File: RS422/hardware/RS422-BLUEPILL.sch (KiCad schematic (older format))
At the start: 9 parts, among them P2 RJ45, P3 RJ45, U1 BLUE-PILL, U2 SN75179, U3 SN75179

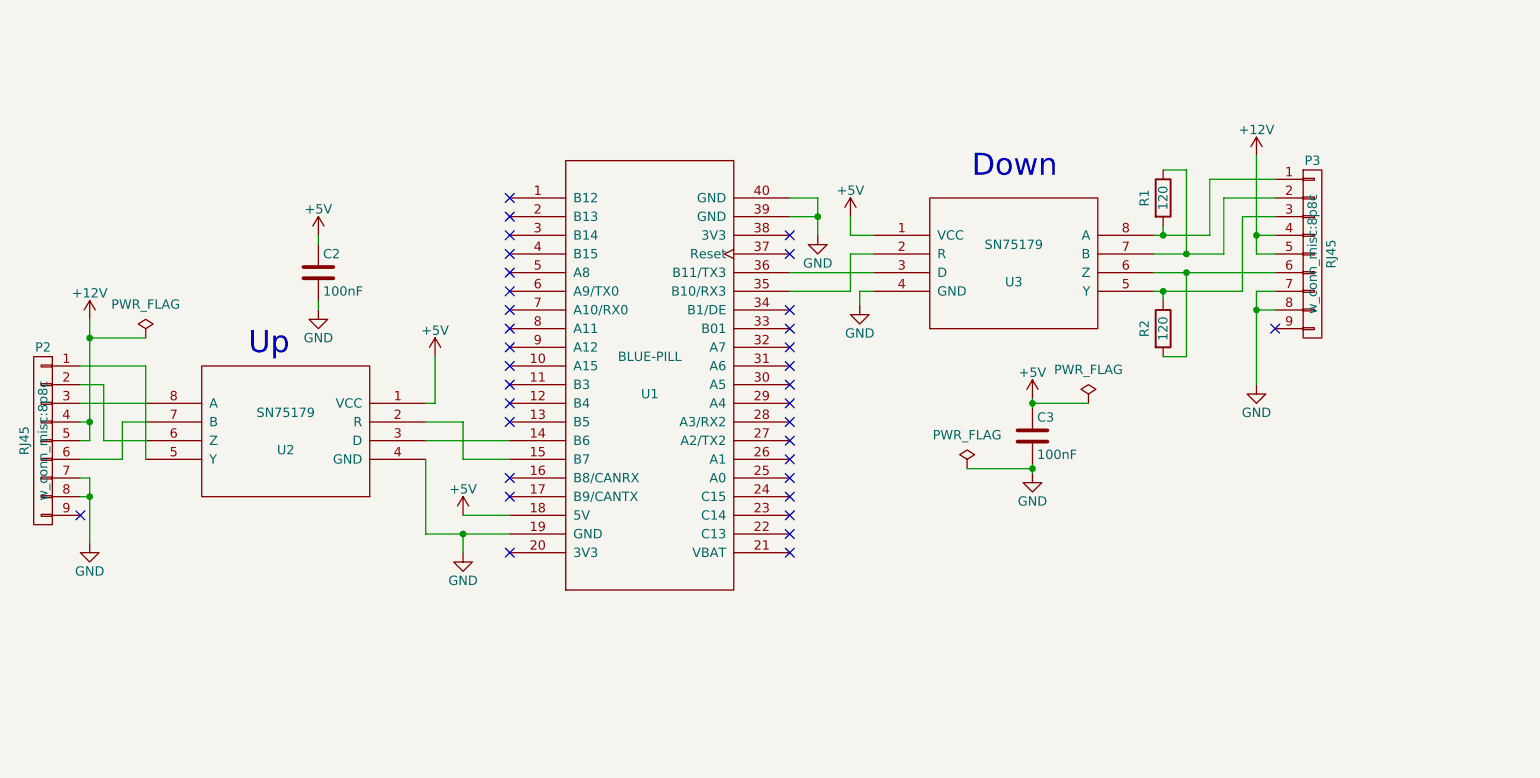
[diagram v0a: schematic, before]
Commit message: assumin first word is always address with 9th bit set
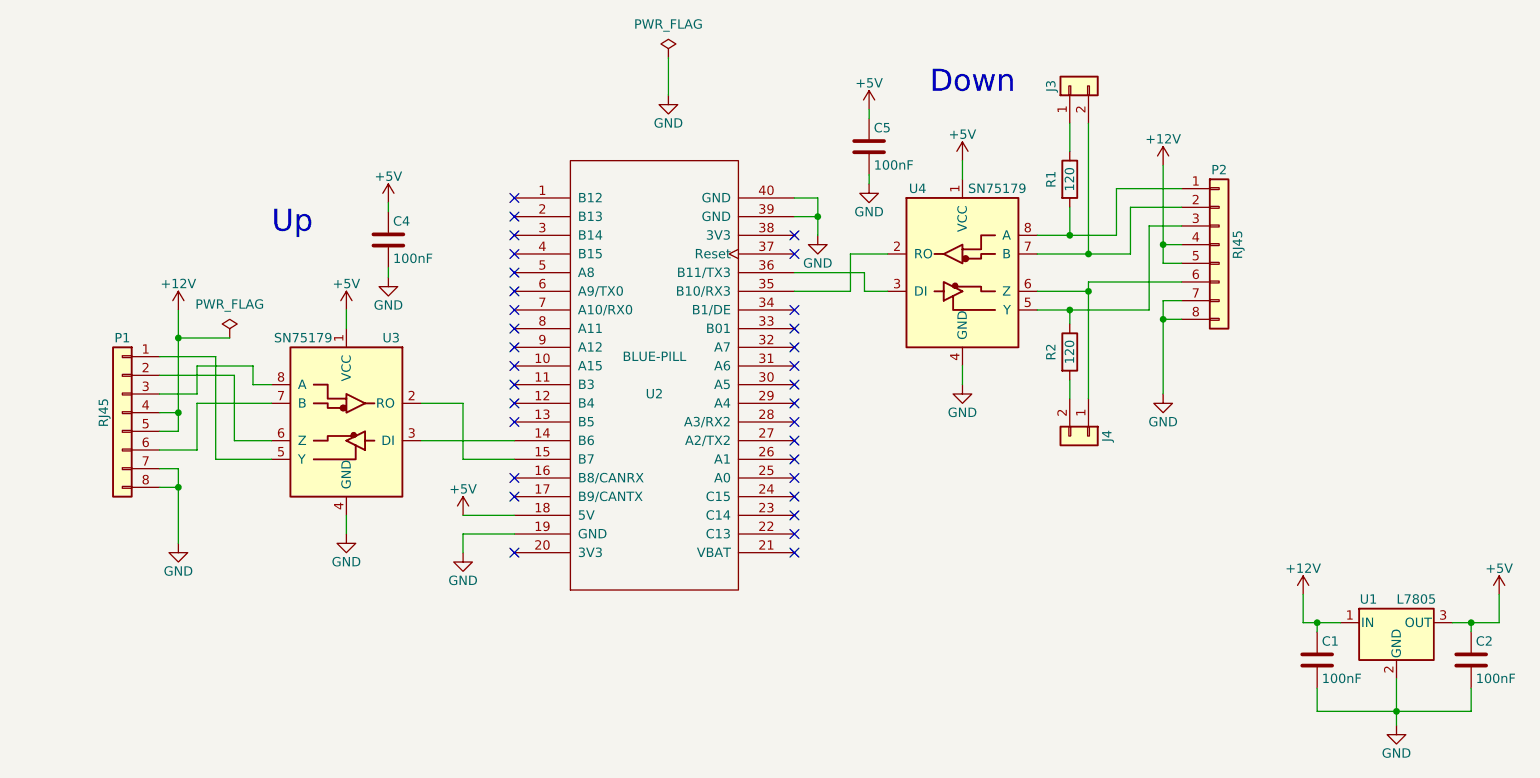
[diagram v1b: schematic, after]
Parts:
- removed P2, P3: RJ45, w_conn_misc:8p8c, symbol CONN_01X09
- removed U2, U3: SN75179, w_pth_circuits:dil_8-300_socket, symbol SN75179
- added C1, C2: 100nF, Capacitors_THT:C_Disc_D3.4mm_W2.1mm_P2.50mm, symbol C
- added J3, J4: Conn_01x02, Pin_Headers:Pin_Header_Straight_1x02_Pitch2.54mm, symbol Conn_01x02
- added P1, P2: RJ45, w_conn_misc:8p8c, symbol Conn_01x08
- added U1: L7805, TO_SOT_Packages_THT:TO-220_Neutral123_Horizontal_LargePads, symbol L7805
- added U3, U4: SN75179, w_pth_circuits:dil_8-300_socket, symbol MAX488E
- C4: renamed from C2; footprint Capacitors_ThroughHole:C_Disc_D3_P2.5 -> Capacitors_THT:C_Disc_D3.4mm_W2.1mm_P2.50mm
- C5: renamed from C3; footprint Capacitors_ThroughHole:C_Disc_D3_P2.5 -> Capacitors_THT:C_Disc_D3.4mm_W2.1mm_P2.50mm
- R1, R2: footprint Resistors_ThroughHole:Resistor_Horizontal_RM7mm -> Resistors_THT:R_Axial_DIN0204_L3.6mm_D1.6mm_P7.62mm_Horizontal
- renumbered U1 to U2
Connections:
- net +12V: now also C1.1, P1.4 (Pin_4), P1.5 (Pin_5), P2.4 (Pin_4), P2.5 (Pin_5), U1.1 (IN)
- net +5V: now also C2.1, U1.3 (OUT), U3.1 (VCC), U4.1 (VCC)
- net GND: now also C1.2, C2.2, P1.7 (Pin_7), P1.8 (Pin_8), P2.7 (Pin_7), P2.8 (Pin_8), U1.2 (GND), U3.4 (GND), U4.4 (GND)
- net at R1.1: now also J3.1 (Pin_1)
- net at R1.2: now also P2.1 (Pin_1), U4.8 (A)
- net at U2.35 (B10/RX3): now also U4.2 (RO)
- net at U2.36 (B11/TX3): now also U4.3 (DI)
- net at R2.1: now also P2.3 (Pin_3), U4.5 (Y)
- net at R2.2: now also J4.2 (Pin_2)
- net at U2.15 (B7): now also U3.2 (RO)
- net at U2.14 (B6): now also U3.3 (DI)
- new net: J4.1 (Pin_1), P2.6 (Pin_6), U4.6 (Z)
- new net: J3.2 (Pin_2), P2.2 (Pin_2), U4.7 (B)
- new net: P1.1 (Pin_1), U3.5 (Y)
- new net: P1.2 (Pin_2), U3.6 (Z)
- new net: P1.6 (Pin_6), U3.7 (B)
- new net: P1.3 (Pin_3), U3.8 (A)
- no-connect marks 34 -> 32
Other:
- moved on the sheet: C4, C5, R1, R2, U2
